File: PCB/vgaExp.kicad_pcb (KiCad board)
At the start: 2 copper layers, 80 x 91.1 mm, 83 parts, among them J1 DE-15, J2 DE-15, J3 VHDCI, U1 ADP3303-3V3, U2 ADP3334, U3 AD9984, U4 ADP3334, U5 24AA014, U6 TCA9617A, U7 TCA9617A

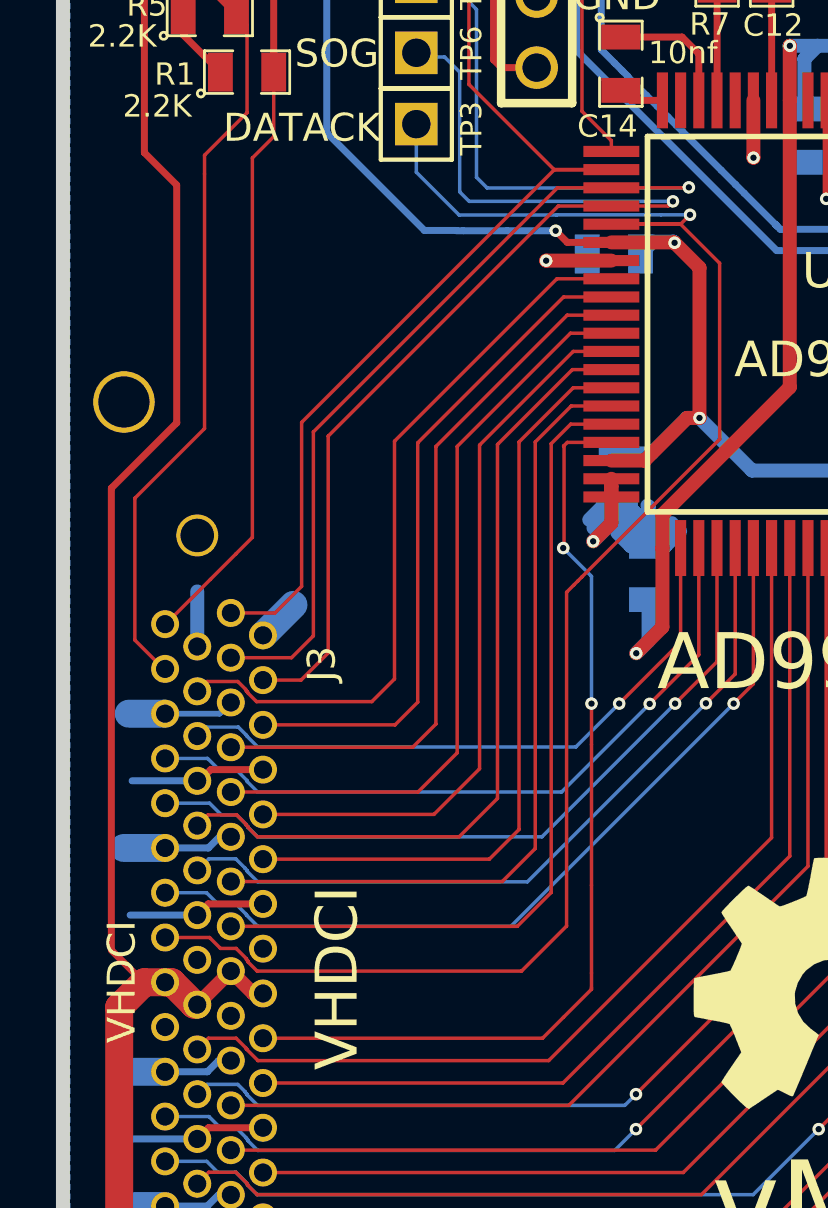
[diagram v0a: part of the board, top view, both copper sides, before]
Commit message: 50% length matched
R[9:0], DATACK, VSOUT, HSOUT, SOGOUT, RGB
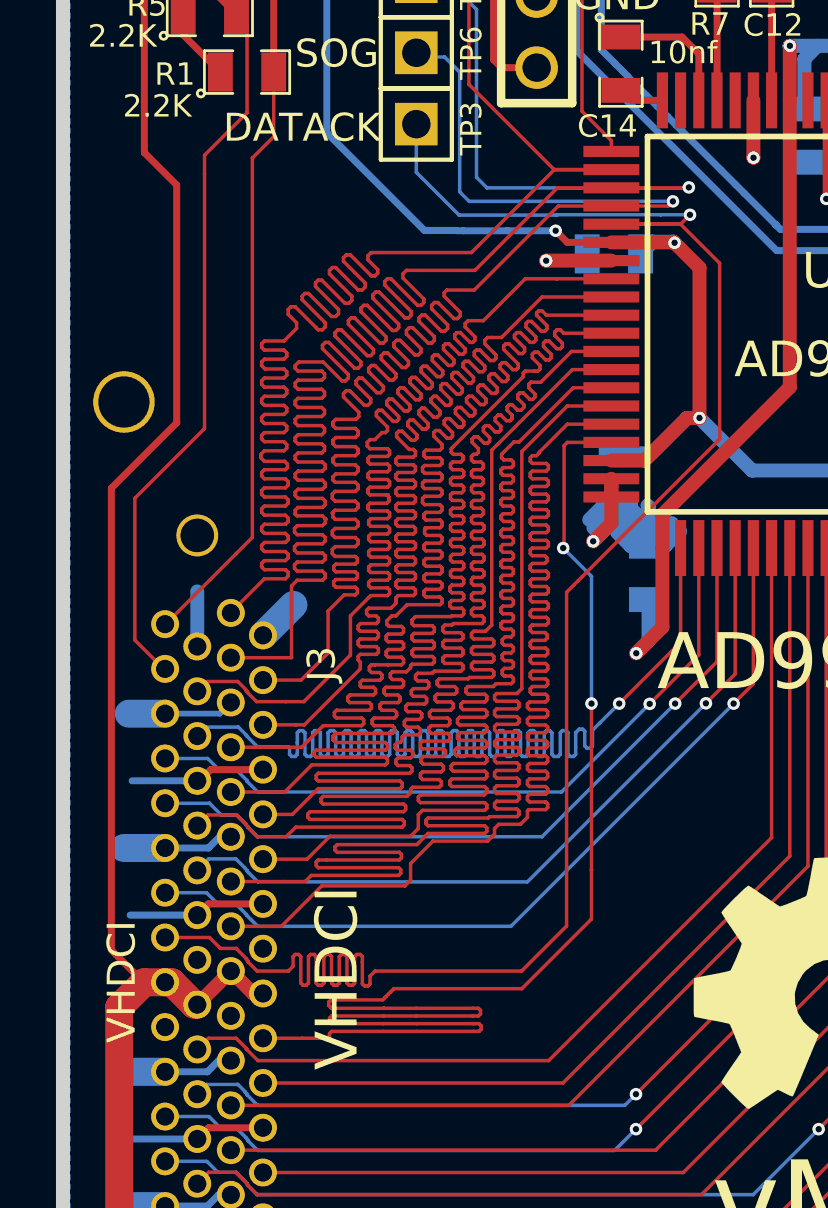
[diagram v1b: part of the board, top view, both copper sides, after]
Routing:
- net /HSOUT: track 43.9 -> 87.5 mm
- net /VSOUT: track 46.1 -> 80.8 mm
- net /G9: track 22.6 -> 54.8 mm
- net /R7: track 25.8 -> 56.9 mm
- net /SOGOUT: track 40.2 -> 70.7 mm
- net /R3: track 27.5 -> 56.3 mm
- net /R6: track 26.8 -> 55.4 mm
- net /R5: track 26.1 -> 53.7 mm
- net /R2: track 29.2 -> 56.4 mm
- net /R4: track 29.6 -> 56.0 mm
- net /R1: track 30.4 -> 55.6 mm
- net /R8: track 24.2 -> 48.1 mm
- net /R9: track 26.5 -> 50.1 mm
- net /R0: track 34.1 -> 54.7 mm
- net /DATACK: track 61.0 -> 71.0 mm

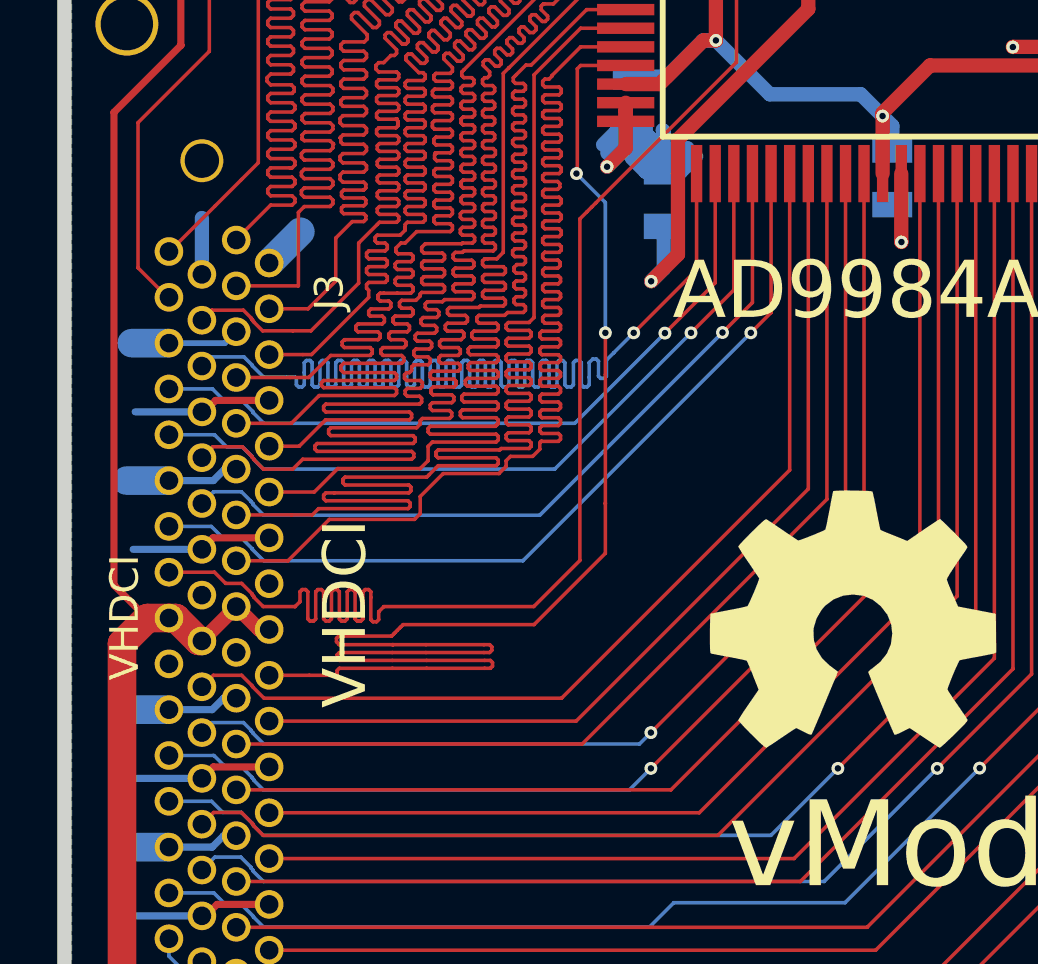
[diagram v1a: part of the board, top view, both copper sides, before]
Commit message: 80% length matching done
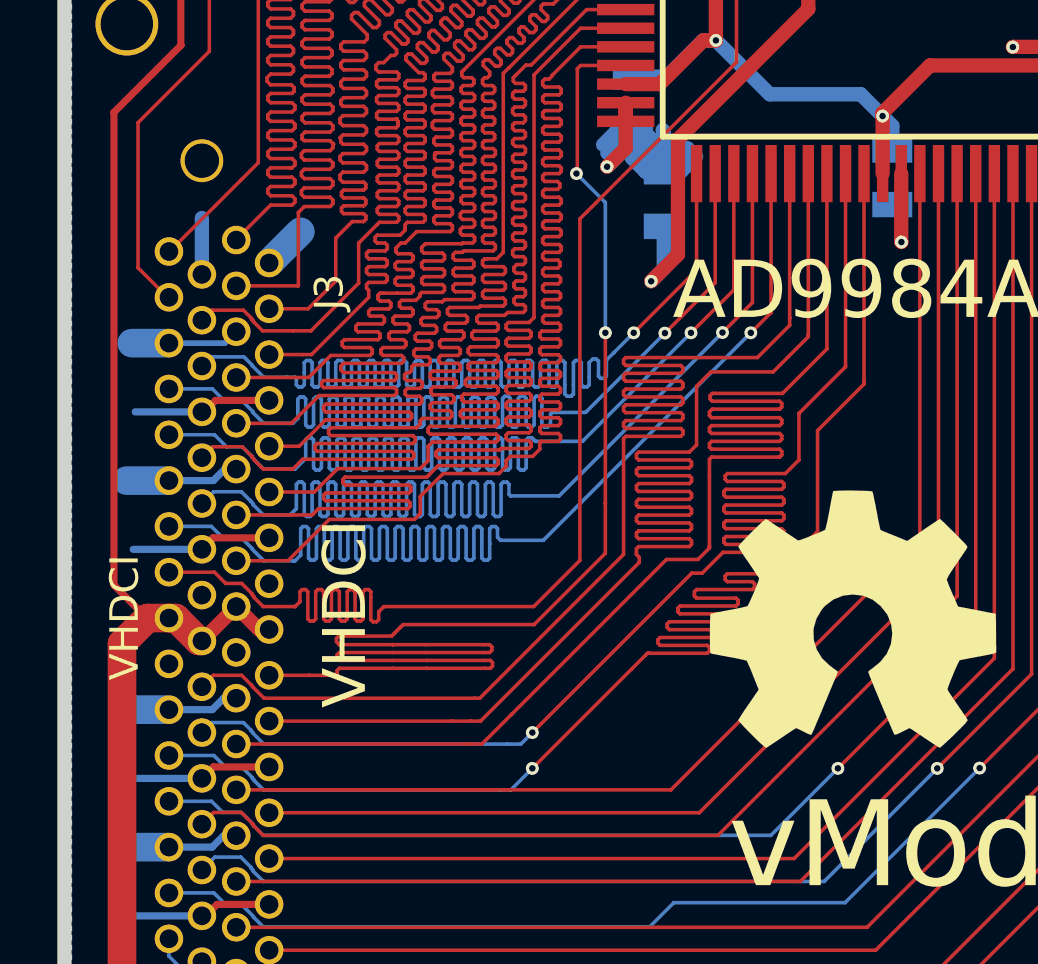
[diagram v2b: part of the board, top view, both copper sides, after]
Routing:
- net /G8: track 25.4 -> 56.4 mm
- net /G6: track 27.3 -> 57.4 mm
- net /G7: track 26.9 -> 56.4 mm
- net /G5: track 30.0 -> 57.2 mm
- net /G3: track 33.2 -> 55.7 mm
- net /G4: track 34.7 -> 55.6 mm
- net /G2: track 35.5 -> 55.1 mm
- net /G1: track 38.7 -> 55.9 mm
- net /G0: track 41.5 -> 56.4 mm
- net /G9: track 54.8 -> 55.5 mm

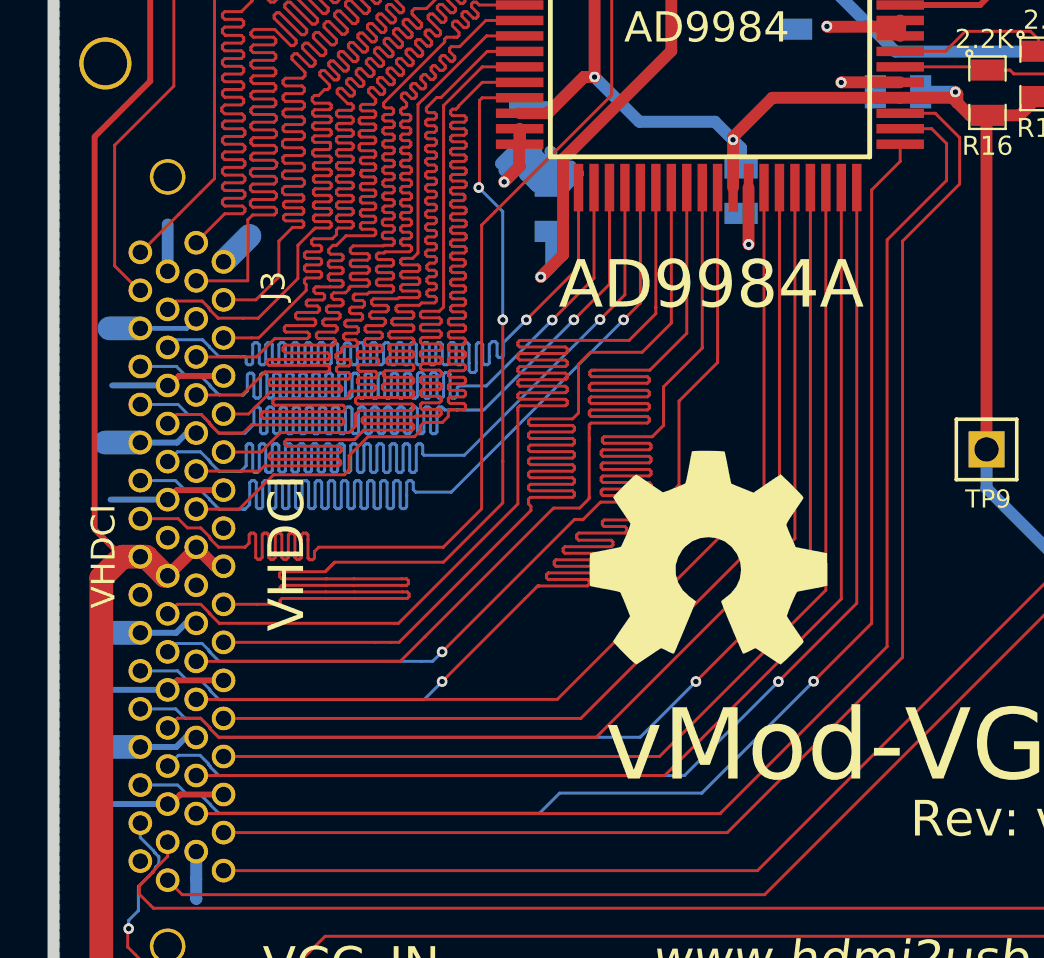
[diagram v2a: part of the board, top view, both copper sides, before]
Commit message: 100% track length-matched
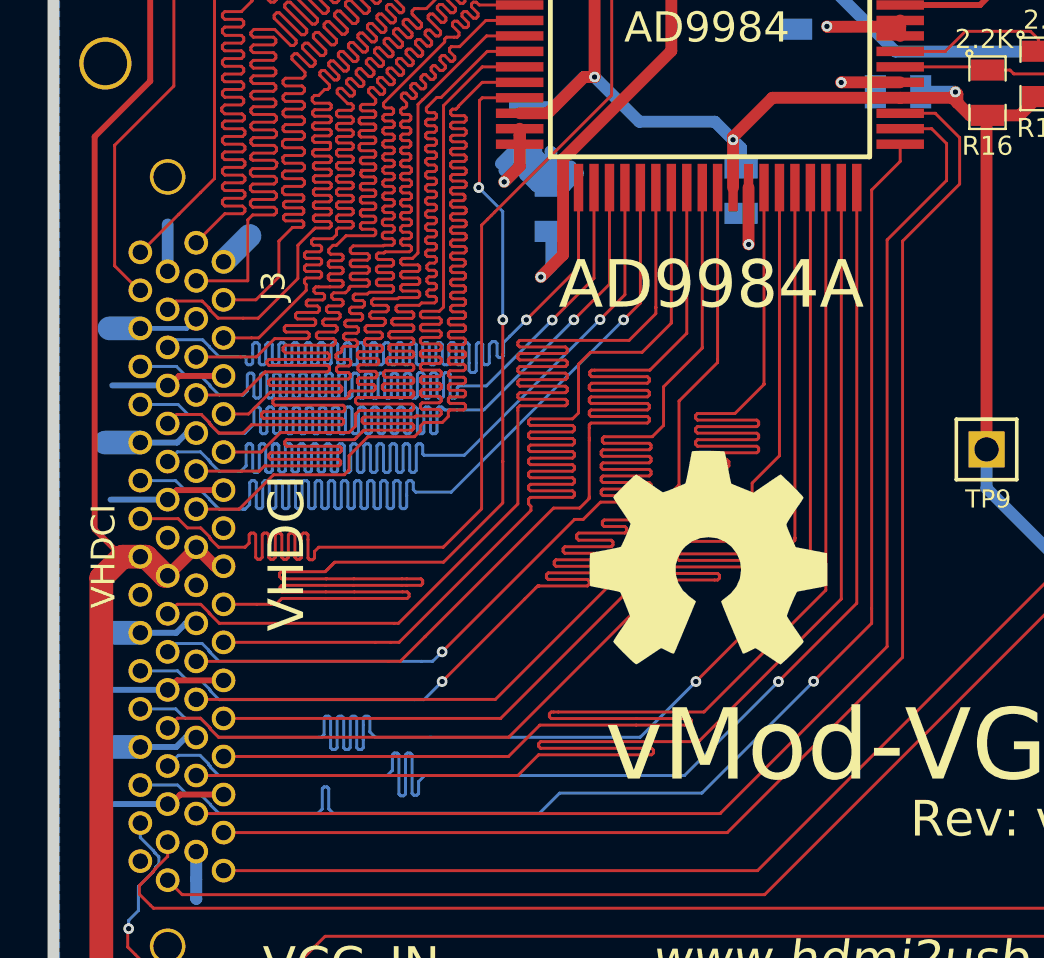
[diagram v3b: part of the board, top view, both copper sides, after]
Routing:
- net /B9: track 40.3 -> 57.0 mm
- net /B8: track 40.8 -> 56.3 mm
- net /B5: track 45.1 -> 57.4 mm
- net /B7: track 45.1 -> 57.2 mm
- net /B4: track 47.5 -> 57.3 mm
- net /B6: track 47.6 -> 57.0 mm
- net /B3: track 50.0 -> 56.6 mm
- net /B2: track 55.2 -> 57.1 mm
- net /R0: track 54.7 -> 55.9 mm

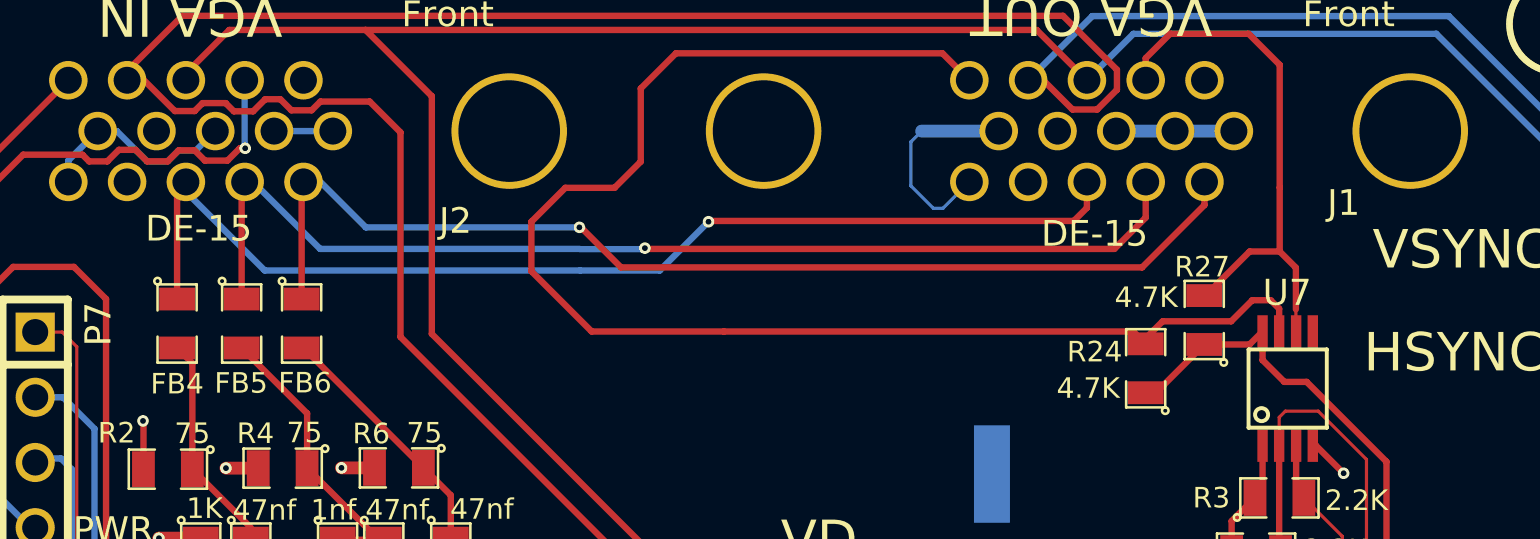
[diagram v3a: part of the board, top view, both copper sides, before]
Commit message: Fixes #22. Fixes #12. Fixes #9
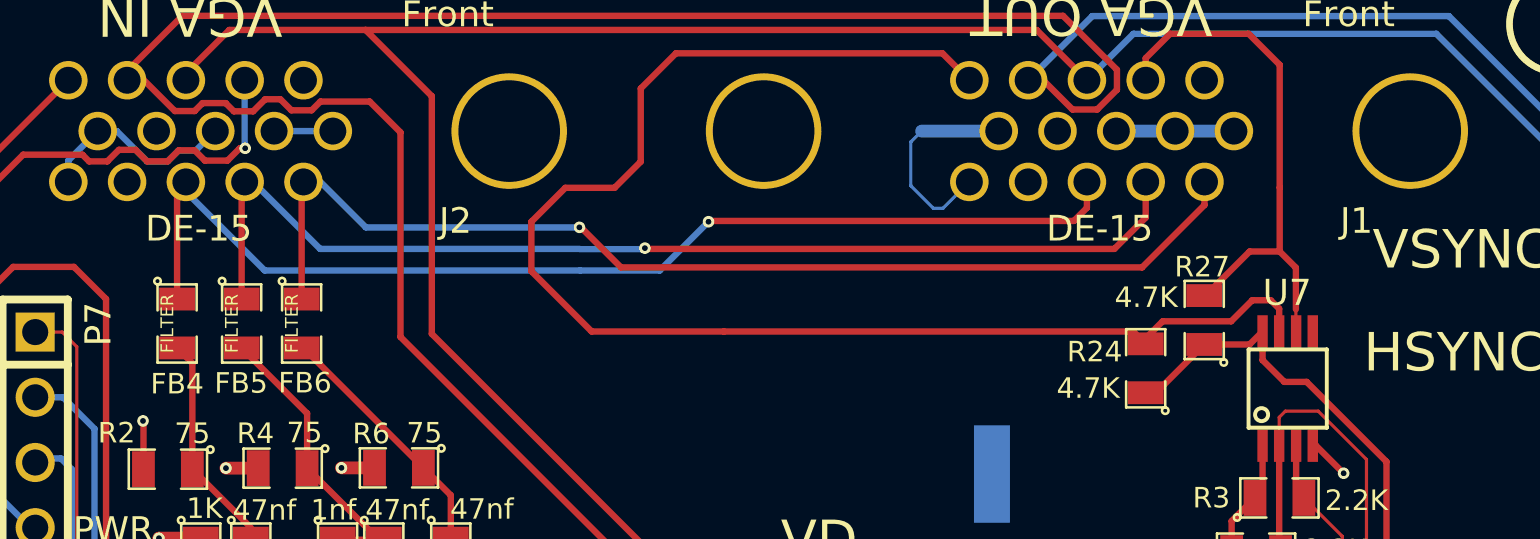
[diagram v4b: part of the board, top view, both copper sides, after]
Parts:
- FB4, FB5, FB6: value (none) -> FILTER
- P5, P6: value (none) -> CONN_1
- P7: value (none) -> CONN_6
- R14: value 147K -> R147K
- TP1, TP10, TP11, TP12, TP13, TP2, TP3, TP4, TP5, TP6, TP7, TP8, TP9: value (none) -> TESTPOINT

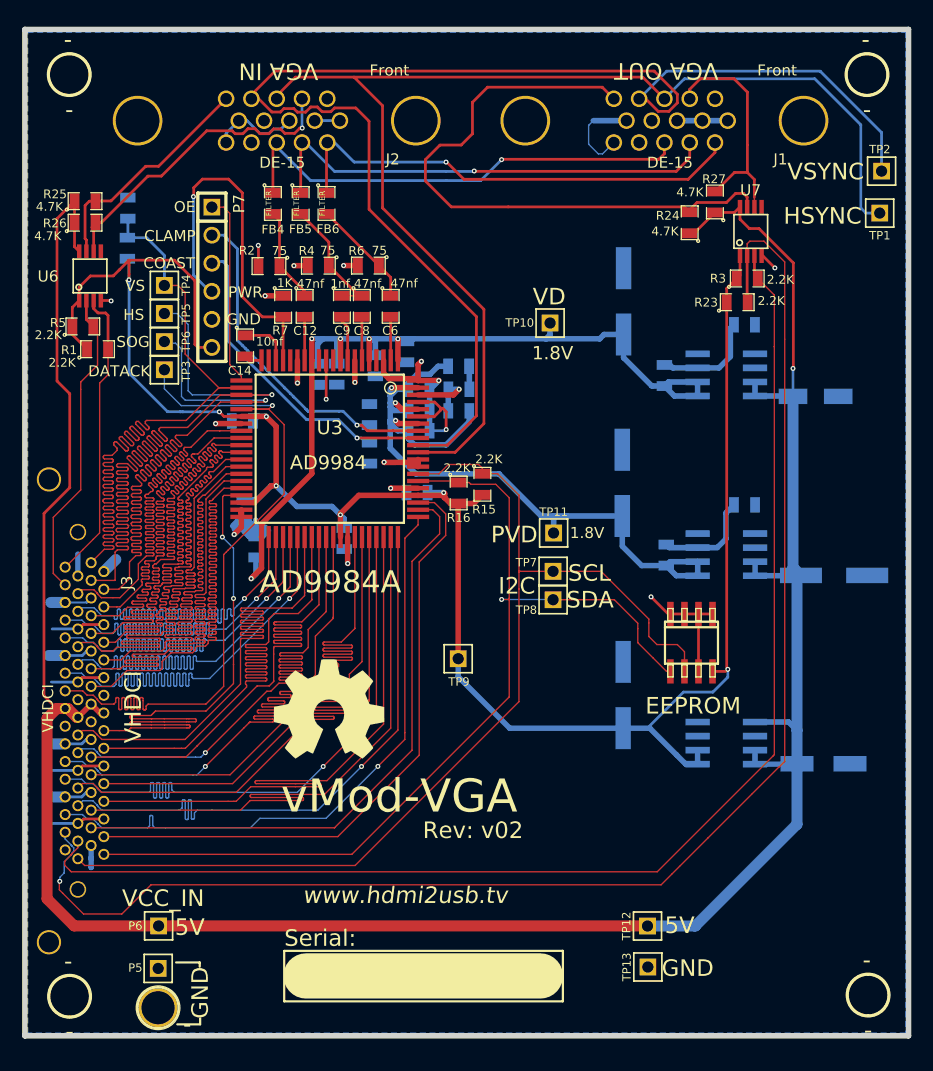
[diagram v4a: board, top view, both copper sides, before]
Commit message: Changed vias to 0.6dia, 0.3drill
Also reduced width of power tracks from IC from 0.500mm toh 0.400mm
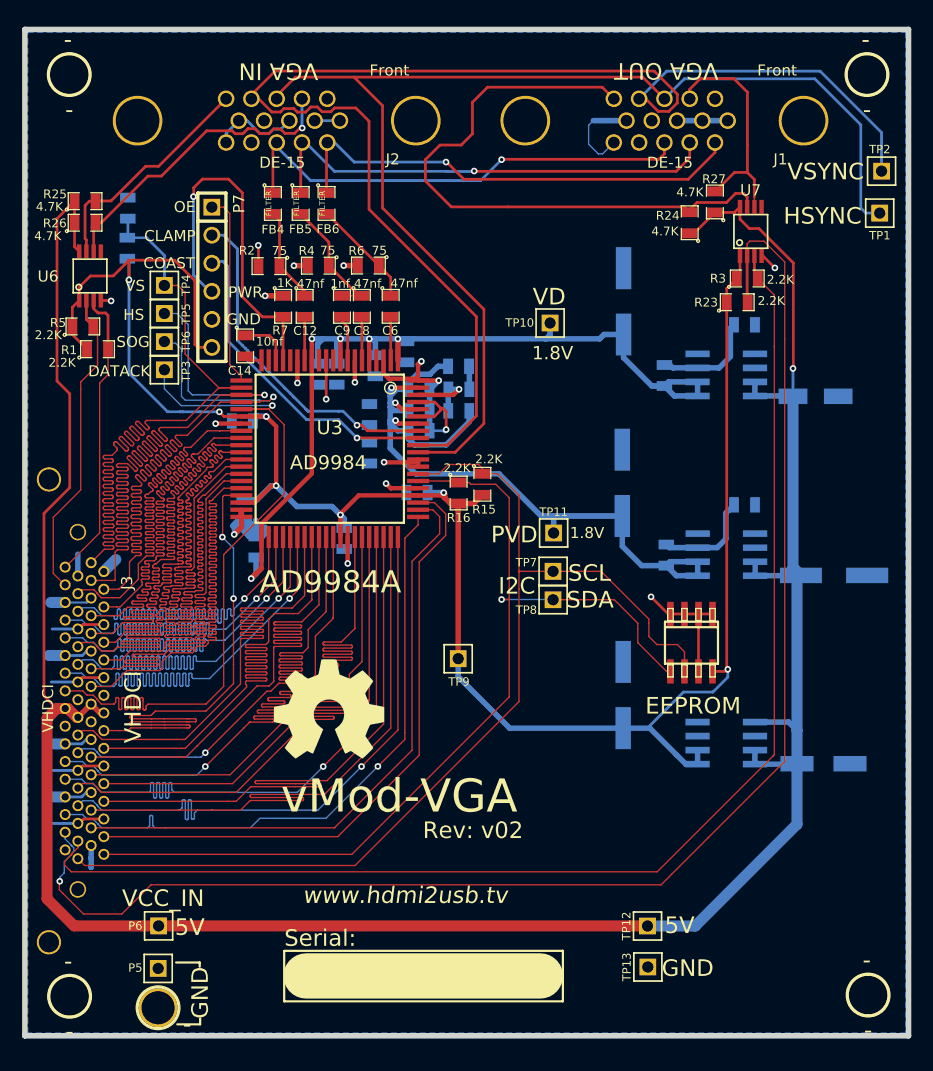
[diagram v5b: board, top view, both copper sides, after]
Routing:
- net /SOGOUT: track 70.7 -> 72.3 mm
- net /HSOUT: track 87.5 -> 86.1 mm
- net /I2C/DDC Section/GND: track 143.2 -> 143.8 mm
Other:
- net class Default: via_dia 0.45 -> 0.6
- rule via_min_size: 0.45 -> 0.6
